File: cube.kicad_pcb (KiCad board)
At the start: 2 copper layers, 300 parts, among them J1 serial_conn, J10 Conn_01x01, J11 Conn_01x01, J2 shifters_common_conn, J3 Conn_01x01, J4 Conn_01x01, J5 Conn_01x01, J6 Conn_01x01, J7 Conn_01x01, J8 Conn_01x01, J9 Conn_01x01, Q1 IRF9540N, Q2 IRF9540N, Q3 IRF9540N, Q4 IRF9540N, Q5 IRF9540N, Q6 IRF9540N, Q7 IRF9540N, Q8 IRF9540N, U1 SN74HC595N_0_b, U10 SN74HC595N_3_b, U11 SN74HC595N_3_g, U12 SN74HC595N_3_r, U13 SN74HC595N_4_b, U14 SN74HC595N_4_g, U15 SN74HC595N_4_r, U16 SN74HC595N_5_b, U17 SN74HC595N_5_g, U18 SN74HC595N_5_r, U19 SN74HC595N_6_b, U2 SN74HC595N_0_g, U20 SN74HC595N_6_g, U21 SN74HC595N_6_r, U22 SN74HC595N_7_b, U23 SN74HC595N_7_g, U24 SN74HC595N_7_r, U25 SN74HC595N_cols, U3 SN74HC595N_0_r, U4 SN74HC595N_1_b, U5 SN74HC595N_1_g, U6 SN74HC595N_1_r, U7 SN74HC595N_2_b, U8 SN74HC595N_2_g, U9 SN74HC595N_2_r

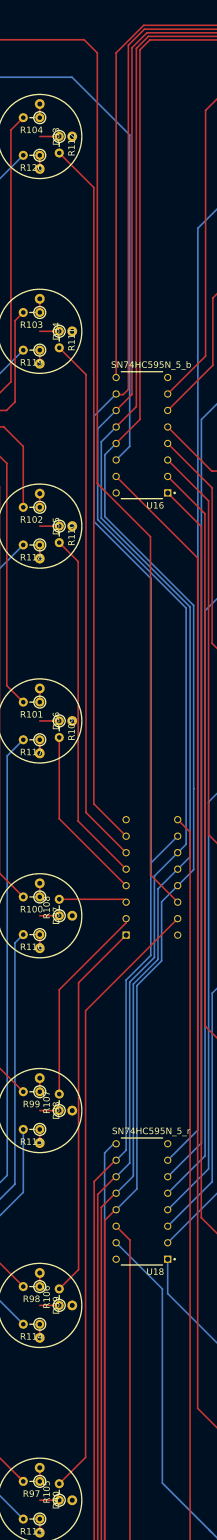
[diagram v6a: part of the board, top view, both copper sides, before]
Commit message: fix 5th rows's green conns
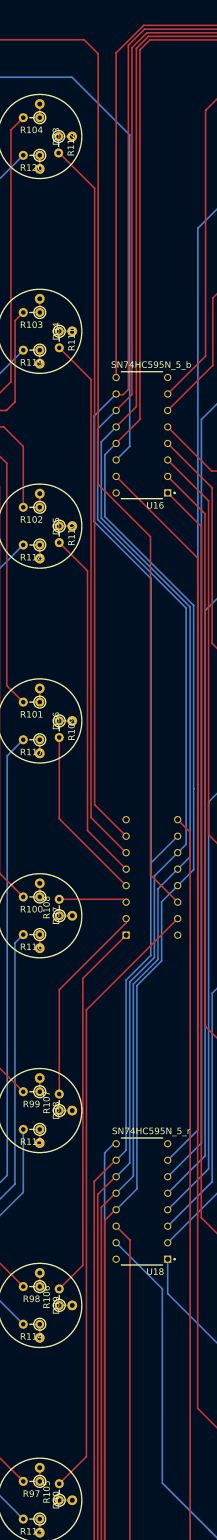
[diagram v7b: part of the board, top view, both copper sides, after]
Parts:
- moved R112 0.10 mm to (170.8, 90.0)
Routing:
- net led_4_7_g: track 3.00 -> 2.00 mm
- net led_4_6_g: track 3.00 -> 2.00 mm
- net led_4_5_g: track 3.00 -> 2.00 mm
- net led_4_4_g: track 3.00 -> 2.00 mm
- net led_4_3_g: track 3.00 -> 2.00 mm
- net led_4_2_g: track 3.00 -> 2.00 mm
- net led_4_1_g: track 3.00 -> 2.00 mm
- net led_4_0_g: track 3.00 -> 2.10 mm
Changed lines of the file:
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@@
   )
   (module Resistor_THT:R_Axial_DIN0204_L3.6mm_D1.6mm_P2.54mm_Vertical (layer F.Cu)
-    (at 170.94 90 270)
+    (at 170.84 90 270)
     (descr "Resistor, Axial_DIN0204 series, Axial, Vertical, pin pitch=2.54mm, 0.167W, length*diameter=3.6*1.6mm^2, http://cdn-reichelt.de/documents/datenblatt/B400/1_4W%23YAG.pdf")
     (tags "Resistor Axial_DIN0204 series Axial Vertical pin pitch 2.54mm 0.167W length 3.6mm diameter 1.6mm")
@@
   (segment (start 148.88601 75.692779) (end 148.88601 121.63181) (width 0.25) (layer F.Cu) (net 211))
   (segment (start 152.0444 124.7902) (end 152.0444 137.6052) (width 0.25) (layer F.Cu) (net 211))
-  (segment (start 176.80071 143.443312) (end 176.80071 77.13111) (width 0.25) (layer F.Cu) (net 212))
-  (segment (start 148.717 141.0462) (end 147.7264 142.0368) (width 0.25) (layer F.Cu) (net 212))
+  (segment (start 176.935433 143.578035) (end 176.935433 77.265833) (width 0.25) (layer F.Cu) (net 212))
   (segment (start 184.9882 203.7006) (end 184.9882 151.630802) (width 0.25) (layer F.Cu) (net 212))
+  (segment (start 155.1972 185.7026) (end 155.1972 195.1796) (width 0.25) (layer F.Cu) (net 212))
+  (segment (start 155.1432 136.8806) (end 150.9776 141.0462) (width 0.25) (layer F.Cu) (net 212))
   (segment (start 150.9776 141.0462) (end 148.717 141.0462) (width 0.25) (layer F.Cu) (net 212))
+  (segment (start 184.9882 151.630802) (end 176.935433 143.578035) (width 0.25) (layer F.Cu) (net 212))
+  (segment (start 176.935433 77.265833) (end 174.7774 75.1078) (width 0.25) (layer F.Cu) (net 212))
+  (segment (start 174.7774 75.1078) (end 157.0228 75.1078) (width 0.25) (layer F.Cu) (net 212))
   (segment (start 157.0228 75.1078) (end 155.1432 76.9874) (width 0.25) (layer F.Cu) (net 212))
-  (segment (start 184.9882 151.630802) (end 176.80071 143.443312) (width 0.25) (layer F.Cu) (net 212))
-  (segment (start 155.1432 136.8806) (end 150.9776 141.0462) (width 0.25) (layer F.Cu) (net 212))
   (segment (start 155.1432 76.9874) (end 155.1432 136.8806) (width 0.25) (layer F.Cu) (net 212))
+  (segment (start 189.1672 207.8796) (end 184.9882 203.7006) (width 0.25) (layer F.Cu) (net 212))
+  (segment (start 148.717 141.0462) (end 147.7264 142.0368) (width 0.25) (layer F.Cu) (net 212))
   (segment (start 147.7264 142.0368) (end 147.7264 178.2318) (width 0.25) (layer F.Cu) (net 212))
-  (segment (start 176.80071 77.13111) (end 174.7774 75.1078) (width 0.25) (layer F.Cu) (net 212))
-  (segment (start 155.1972 185.7026) (end 155.1972 195.1796) (width 0.25) (layer F.Cu) (net 212))
   (segment (start 147.7264 178.2318) (end 155.1972 185.7026) (width 0.25) (layer F.Cu) (net 212))
-  (segment (start 174.7774 75.1078) (end 157.0228 75.1078) (width 0.25) (layer F.Cu) (net 212))
-  (segment (start 189.1672 207.8796) (end 184.9882 203.7006) (width 0.25) (layer F.Cu) (net 212))
   (segment (start 147.447 311.0738) (end 147.447 259.999401) (width 0.25) (layer B.Cu) (net 213))
   (segment (start 115.7172 245.0592) (end 114.173 246.6034) (width 0.25) (layer B.Cu) (net 213))
@@
   (segment (start 163.5 89) (end 163.5 127.774999) (width 0.25) (layer F.Cu) (net 221))
   (segment (start 165.4 87.1) (end 163.5 89) (width 0.25) (layer F.Cu) (net 221))
-  (segment (start 174.9935 224.6315) (end 189.18 210.445) (width 0.25) (layer F.Cu) (net 222))
-  (segment (start 174.9935 293.4065) (end 174.9935 224.6315) (width 0.25) (layer F.Cu) (net 222))
-  (segment (start 170.94 297.46) (end 174.9935 293.4065) (width 0.25) (layer F.Cu) (net 222))
-  (segment (start 173.914 220.311) (end 181.24 212.985) (width 0.25) (layer F.Cu) (net 223))
-  (segment (start 173.914 264.486) (end 173.914 220.311) (width 0.25) (layer F.Cu) (net 223))
-  (segment (start 170.94 267.46) (end 173.914 264.486) (width 0.25) (layer F.Cu) (net 223))
+  (segment (start 175.124211 224.500789) (end 189.18 210.445) (width 0.25) (layer F.Cu) (net 222))
+  (segment (start 175.124211 293.275789) (end 175.124211 224.500789) (width 0.25) (layer F.Cu) (net 222))
+  (segment (start 170.94 297.46) (end 175.124211 293.275789) (width 0.25) (layer F.Cu) (net 222))
+  (segment (start 174.5742 219.6508) (end 181.24 212.985) (width 0.25) (layer F.Cu) (net 223))
+  (segment (start 174.5742 263.8258) (end 174.5742 219.6508) (width 0.25) (layer F.Cu) (net 223))
+  (segment (start 170.94 267.46) (end 174.5742 263.8258) (width 0.25) (layer F.Cu) (net 223))
   (segment (start 181.24 211.089998) (end 181.24 210.445) (width 0.25) (layer F.Cu) (net 224))
   (segment (start 170.94 221.389998) (end 181.24 211.089998) (width 0.25) (layer F.Cu) (net 224))
@@
   (segment (start 170.94 195.065) (end 181.24 205.365) (width 0.25) (layer F.Cu) (net 226))
   (segment (start 170.94 182.54) (end 170.94 195.065) (width 0.25) (layer F.Cu) (net 226))
-  (segment (start 173.8505 195.4355) (end 181.24 202.825) (width 0.25) (layer F.Cu) (net 227))
-  (segment (start 173.8505 155.4505) (end 173.8505 195.4355) (width 0.25) (layer F.Cu) (net 227))
-  (segment (start 170.94 152.54) (end 173.8505 155.4505) (width 0.25) (layer F.Cu) (net 227))
-  (segment (start 175.057 194.102) (end 181.24 200.285) (width 0.25) (layer F.Cu) (net 228))
-  (segment (start 175.057 126.657) (end 175.057 194.102) (width 0.25) (layer F.Cu) (net 228))
-  (segment (start 170.94 122.54) (end 175.057 126.657) (width 0.25) (layer F.Cu) (net 228))
-  (segment (start 176.2635 192.7685) (end 181.24 197.745) (width 0.25) (layer F.Cu) (net 229))
-  (segment (start 176.2635 97.8635) (end 176.2635 192.7685) (width 0.25) (layer F.Cu) (net 229))
-  (segment (start 170.94 92.54) (end 176.2635 97.8635) (width 0.25) (layer F.Cu) (net 229))
+  (segment (start 170.94 152.54) (end 175.2854 156.8854) (width 0.25) (layer F.Cu) (net 227))
+  (segment (start 175.2854 196.8704) (end 181.24 202.825) (width 0.25) (layer F.Cu) (net 227))
+  (segment (start 175.2854 156.8854) (end 175.2854 196.8704) (width 0.25) (layer F.Cu) (net 227))
+  (segment (start 175.835411 127.435411) (end 175.835411 194.880411) (width 0.25) (layer F.Cu) (net 228))
+  (segment (start 170.94 122.54) (end 175.835411 127.435411) (width 0.25) (layer F.Cu) (net 228))
+  (segment (start 175.835411 194.880411) (end 181.24 200.285) (width 0.25) (layer F.Cu) (net 228))
+  (segment (start 170.94 92.54) (end 176.385422 97.985422) (width 0.25) (layer F.Cu) (net 229))
+  (segment (start 176.385422 97.985422) (end 176.385422 192.890422) (width 0.25) (layer F.Cu) (net 229))
+  (segment (start 176.385422 192.890422) (end 181.24 197.745) (width 0.25) (layer F.Cu) (net 229))
   (segment (start 156.5785 267.2285) (end 149.7 260.35) (width 0.25) (layer B.Cu) (net 230))
   (segment (start 156.5785 294.078499) (end 156.5785 267.2285) (width 0.25) (layer B.Cu) (net 230))
@@
   (segment (start 261.909999 98.48) (end 256.257959 104.13204) (width 0.25) (layer B.Cu) (net 309))
   (segment (start 167.94 95) (end 167.94 92.9) (width 0.25) (layer F.Cu) (net 310))
-  (segment (start 167.94 90) (end 170.94 90) (width 0.25) (layer F.Cu) (net 311))
+  (segment (start 172.94 90) (end 170.84 90) (width 0.25) (layer F.Cu) (net 311))
   (segment (start 167.94 87.1) (end 167.94 85) (width 0.25) (layer F.Cu) (net 312))
   (segment (start 167.94 125) (end 167.94 122.9) (width 0.25) (layer F.Cu) (net 313))
-  (segment (start 167.94 120) (end 170.94 120) (width 0.25) (layer F.Cu) (net 314))
+  (segment (start 172.94 120) (end 170.94 120) (width 0.25) (layer F.Cu) (net 314))
   (segment (start 167.94 117.1) (end 167.94 115) (width 0.25) (layer F.Cu) (net 315))
   (segment (start 167.94 155) (end 167.94 152.9) (width 0.25) (layer F.Cu) (net 316))
-  (segment (start 170.94 150) (end 167.94 150) (width 0.25) (layer F.Cu) (net 317))
+  (segment (start 172.94 150) (end 170.94 150) (width 0.25) (layer F.Cu) (net 317))
   (segment (start 167.94 147.1) (end 167.94 145) (width 0.25) (layer F.Cu) (net 318))
   (segment (start 167.94 185) (end 167.94 182.9) (width 0.25) (layer F.Cu) (net 319))
-  (segment (start 170.94 180) (end 167.94 180) (width 0.25) (layer F.Cu) (net 320))
+  (segment (start 172.94 180) (end 170.94 180) (width 0.25) (layer F.Cu) (net 320))
   (segment (start 167.94 177.1) (end 167.94 175) (width 0.25) (layer F.Cu) (net 321))
   (segment (start 167.940001 215) (end 167.940001 212.9) (width 0.25) (layer F.Cu) (net 322))
-  (segment (start 170.94 210) (end 167.94 210) (width 0.25) (layer F.Cu) (net 323))
+  (segment (start 172.940001 210) (end 170.940001 210) (width 0.25) (layer F.Cu) (net 323))
   (segment (start 167.940001 207.1) (end 167.940001 205) (width 0.25) (layer F.Cu) (net 324))
   (segment (start 167.940001 245) (end 167.940001 242.9) (width 0.25) (layer F.Cu) (net 325))
-  (segment (start 170.94 240) (end 167.94 240) (width 0.25) (layer F.Cu) (net 326))
+  (segment (start 172.940001 240) (end 170.940001 240) (width 0.25) (layer F.Cu) (net 326))
   (segment (start 167.940001 237.1) (end 167.940001 235) (width 0.25) (layer F.Cu) (net 327))
   (segment (start 167.940001 275) (end 167.940001 272.9) (width 0.25) (layer F.Cu) (net 328))
-  (segment (start 167.94 270) (end 170.94 270) (width 0.25) (layer F.Cu) (net 329))
+  (segment (start 172.940001 270) (end 170.940001 270) (width 0.25) (layer F.Cu) (net 329))
   (segment (start 167.940001 267.1) (end 167.940001 265) (width 0.25) (layer F.Cu) (net 330))
   (segment (start 167.940001 305) (end 167.940001 302.9) (width 0.25) (layer F.Cu) (net 331))
-  (segment (start 167.94 300) (end 170.94 300) (width 0.25) (layer F.Cu) (net 332))
+  (segment (start 172.940001 300) (end 170.940001 300) (width 0.25) (layer F.Cu) (net 332))
   (segment (start 167.940001 297.1) (end 167.940001 295) (width 0.25) (layer F.Cu) (net 333))
   (segment (start 181.788 137.722) (end 179.7 139.81) (width 0.25) (layer B.Cu) (net 334))

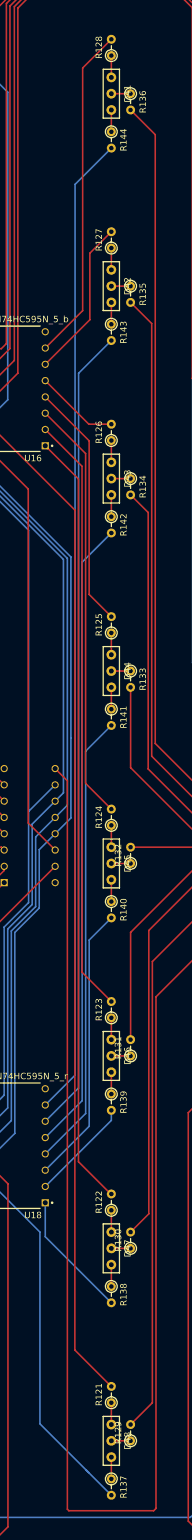
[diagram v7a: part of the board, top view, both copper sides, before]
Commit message: fix 6th rows's red conns
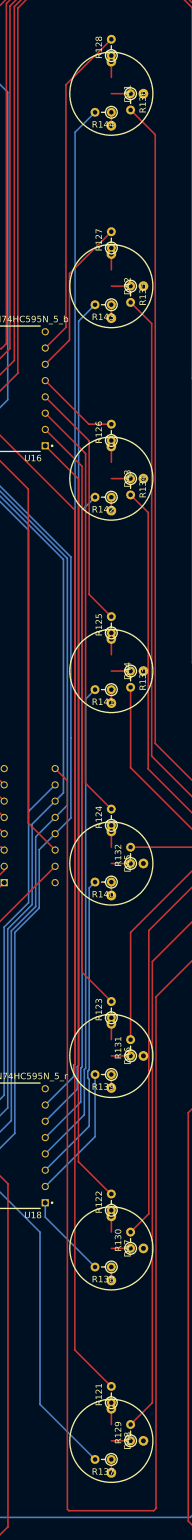
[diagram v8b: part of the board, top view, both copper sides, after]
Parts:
- moved R137 3.04 mm to (197.9, 302.9), turned to 180 degrees
- moved R138 3.04 mm to (197.9, 272.9), turned to 180 degrees
- moved R139 3.04 mm to (197.9, 242.9), turned to 180 degrees
- moved R140 3.04 mm to (197.9, 212.9), turned to 180 degrees
- moved R141 3.04 mm to (197.9, 182.9), turned to 180 degrees
- moved R142 3.04 mm to (197.9, 152.9), turned to 180 degrees
- moved R143 3.04 mm to (197.9, 122.9), turned to 180 degrees
- moved R144 3.04 mm to (197.9, 92.9), turned to 180 degrees
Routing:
- net Net-(R137-Pad2): track 56.3 -> 49.1 mm
- net Net-(R138-Pad2): track 19.9 -> 13.2 mm
- net Net-(R140-Pad2): track 43.6 -> 48.3 mm
- net Net-(R139-Pad2): track 16.1 -> 20.7 mm
- net Net-(R143-Pad2): track 126.0 -> 130.5 mm
- net Net-(R144-Pad2): track 153.4 -> 158.0 mm
- net Net-(R141-Pad2): track 71.1 -> 75.6 mm
- net Net-(R142-Pad2): track 98.5 -> 103.0 mm
- net led_5_5_r: track 3.40 -> 2.10 mm
- net led_5_4_r: track 3.40 -> 2.10 mm
- net led_5_3_r: track 3.40 -> 2.10 mm
- net led_5_2_r: track 3.40 -> 2.10 mm
- net led_5_1_r: track 3.40 -> 2.10 mm
- net led_5_0_r: track 3.40 -> 2.10 mm
- net led_5_7_r: track 3.40 -> 2.10 mm
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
